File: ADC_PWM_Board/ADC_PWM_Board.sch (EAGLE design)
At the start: 52 parts, among them J1 22-05-7028-02, J10 22-05-7028-02, J11 22-05-7038-03, J2 22-05-7028-02, J3 22-05-7048-04, J4 22-05-7048-04, J5 22-05-7048-04, J6 22-05-7038-03, J7 22-05-7048-04, J8 22-05-7058-05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

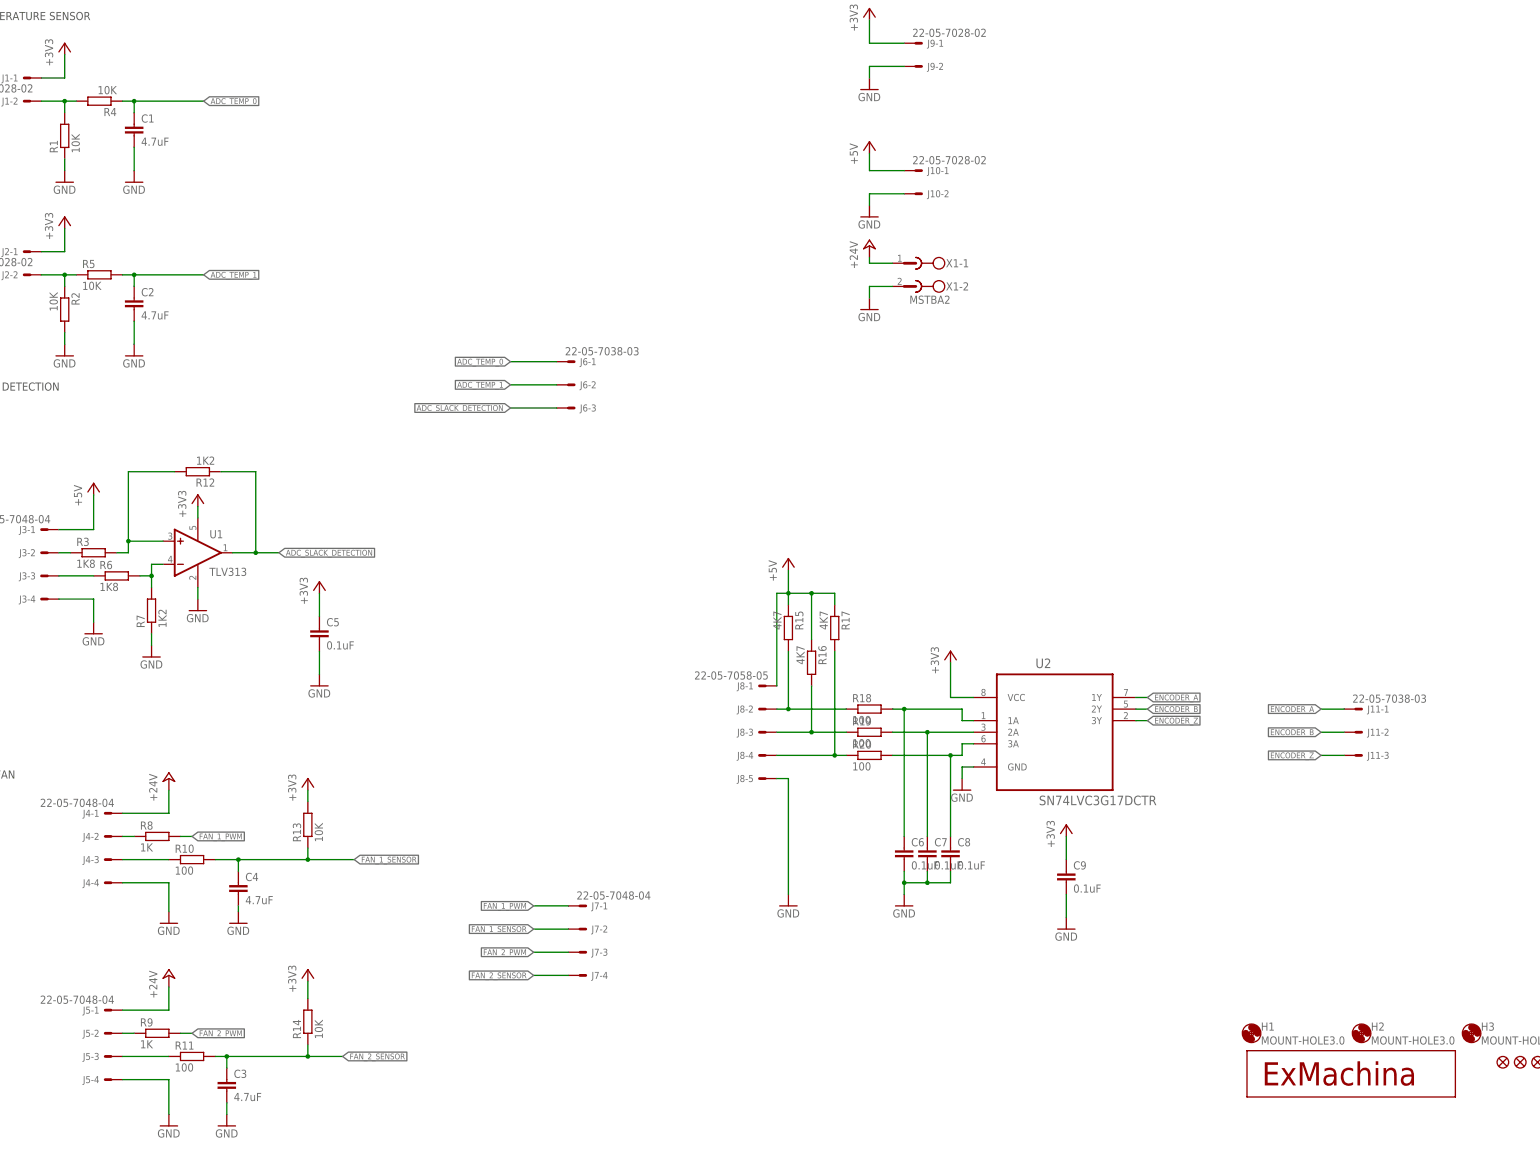
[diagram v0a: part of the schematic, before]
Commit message: Add opto to the Fan sensor and finsh to route it
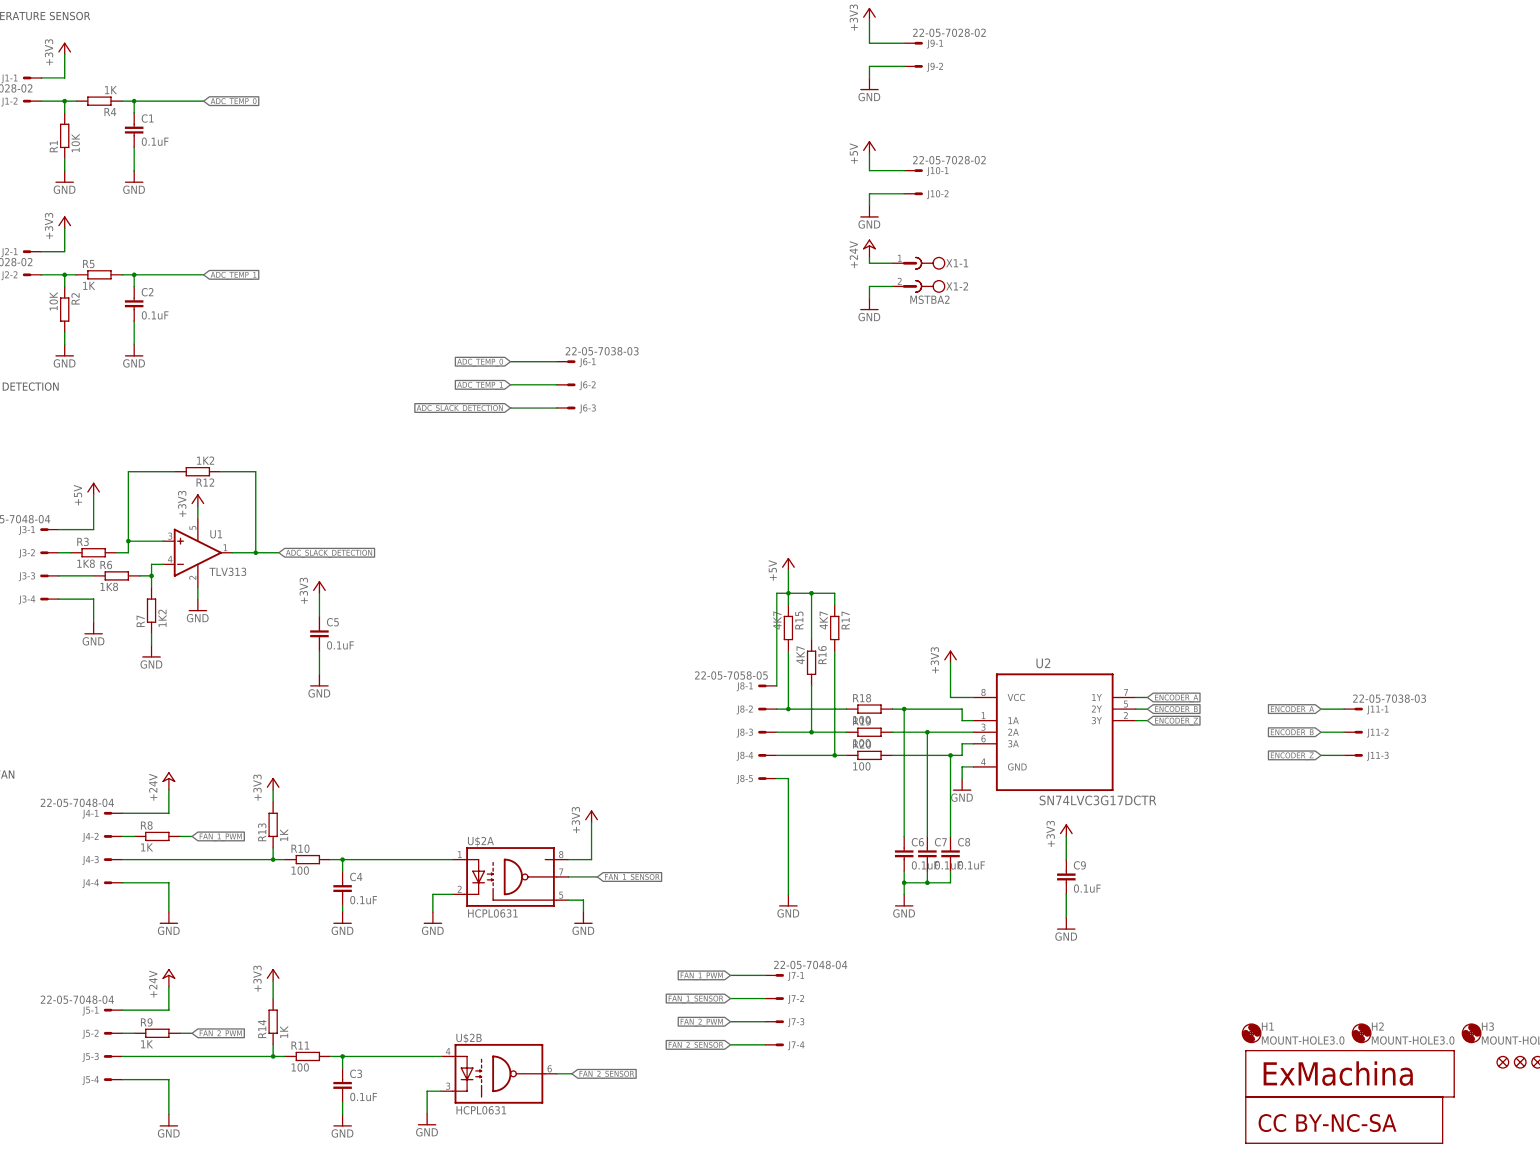
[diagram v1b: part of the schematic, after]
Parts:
- added U$1: CC-BY-NC-SA, cc-by-sa:CC-BY-NC-SA
- added U$2: HCPL0631, optocoupler:HCPL0631
- C1, C2, C3, C4: value 4.7uF -> 0.1uF
- R13, R14, R4, R5: value 10K -> 1K
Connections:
- removed net N$12: J5-3.S, R11.1
- removed net N$14: J4-3.S, R10.1
- new net N$1: J4-3.S, R10.1, R13.1
- new net N$2: J5-3.S, R11.1, R14.1
- new net N$3: C4.1, R10.2, U$2A.A1
- new net N$4: C3.1, R11.2, U$2B.A2
- net +3V3: now also U$2A.VCC
- net FAN_1_SENSOR: now also U$2A.VO; no longer C4.1, R10.2, R13.1
- net FAN_2_SENSOR: now also U$2B.VO2; no longer C3.1, R11.2, R14.1
- net GND: now also U$2A.C1, U$2A.GND, U$2B.C2
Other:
- moved on the sheet: C3, C4, J7-1, J7-2, J7-3, J7-4, R10, R11, R13, R14

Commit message: Add decoupling capacitor to the opto
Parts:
- C1, C2, C3, C4, C5, C6, C7, C8, C9: MPN (none) -> MC0603B104K250CT; OC_NEWARK (none) -> 06R4925
- H1, H2, H3, H4, JP1, JP2, JP3, JP4, T1, U$1: OC_NEWARK (none) -> unknown
- R1, R2: MPN (none) -> MCMR06X1002FTL; OC_NEWARK (none) -> 86T3506
- R10, R11, R18, R19, R20: MPN (none) -> MCMR06X1000FTL; OC_NEWARK (none) -> 86T3504
- R12, R7: MPN (none) -> MCMR06X1201FTL; OC_NEWARK (none) -> 86T3525
- R13, R14, R4, R5, R8, R9: MPN (none) -> MCMR06X1001FTL; OC_NEWARK (none) -> 86T3505
- R15, R16, R17: MPN (none) -> MCMR06X4701FTL; OC_NEWARK (none) -> 86T3649
- R3, R6: MPN (none) -> MCMR06X1801FTL; OC_NEWARK (none) -> 86T3556
- U$2: MPN (none) -> HCPL-0631-500E; OC_NEWARK (none) -> 52M7944
- U1: MPN (none) -> TLV313IDBVT; OC_NEWARK (none) -> 95Y0395
- U2: MF (none) -> TEXAS INSTRUMENTS

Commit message: Replacing name and value on the board
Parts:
- removed U$2: HCPL0631, optocoupler:HCPL0631
- removed X1: MSTBA2, con-phoenix-508:MSTBA2
- added C10: 0.1uF, rcl:C-EUC0603
- added J12: 22-05-7038-03, con-molex:22-05-7038-03
- added U3: SN74LVC3G17DCTR, ti:SN74LVC3G17DCTR
- J1, J10, J2, J9: MPN (none) -> 22-05-7028; OC_NEWARK (none) -> 25M1728
- J11: value 22-05-7038-03 -> MSTBA2; device con-molex:22-05-7038-03 -> con-phoenix-508:MSTBA2
- J3, J4, J5: MPN (none) -> 22-05-7048; OC_NEWARK (none) -> 26M6363
- J6: MPN (none) -> 22-05-7038; OC_NEWARK (none) -> 26M6362
- J7: value 22-05-7048-04 -> 22-05-7058-05; device con-molex:22-05-7048-04 -> con-molex:22-05-7058-05; MF (none) -> MOLEX; MPN (none) -> 22-05-7058; OC_NEWARK (none) -> 55H9619
- J8: value 22-05-7058-05 -> 22-05-7048-04; device con-molex:22-05-7058-05 -> con-molex:22-05-7048-04; MPN (none) -> 22-05-7048; OC_NEWARK (none) -> 26M6363
- R10: value 100 -> 1K2; MPN MCMR06X1000FTL -> MCMR06X1201FTL; OC_NEWARK 86T3504 -> 86T3525
- R11: value 100 -> 1K; MPN MCMR06X1000FTL -> MCMR06X1001FTL; OC_NEWARK 86T3504 -> 86T3505
- R12: value 1K2 -> 1K; MPN MCMR06X1201FTL -> MCMR06X1001FTL; OC_NEWARK 86T3525 -> 86T3505
- R13, R14: value 1K -> 100; MPN MCMR06X1001FTL -> MCMR06X1000FTL; OC_NEWARK 86T3505 -> 86T3504
- U2: value SN74LVC3G17DCTR -> HCPL0631; device ti:SN74LVC3G17DCTR -> optocoupler:HCPL0631; MF TEXAS INSTRUMENTS -> (none); MPN (none) -> HCPL-0631-500E; OC_NEWARK (none) -> 52M7944
- renumbered U$1 to CC1
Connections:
- net +24V: now also J11-1.1; no longer X1-1.1
- net +3V3: now also C10.1, C3.1, C6.1, R11.2, R12.2, U2A.VCC, U3.VCC; no longer C5.1, C9.1, R13.2, R14.2, U$2A.VCC, U2.VCC
- net +5V: now also J7-1.S; no longer J8-1.S
- net ADC_SLACK_DETECTION: now also R10.1; no longer R12.1
- net ENCODER_A: now also J12-1.S, U3.1Y; no longer J11-1.S, U2.1Y
- net ENCODER_B: now also J12-2.S, U3.2Y; no longer J11-2.S, U2.2Y
- net ENCODER_Z: now also J12-3.S, U3.3Y; no longer J11-3.S, U2.3Y
- net FAN_1_PWM: now also J8-1.S; no longer J7-1.S
- net FAN_1_SENSOR: now also J8-2.S, U2A.VO; no longer J7-2.S, U$2A.VO
- net FAN_2_PWM: now also J8-3.S; no longer J7-3.S
- net FAN_2_SENSOR: now also J8-4.S, U2B.VO2; no longer J7-4.S, U$2B.VO2
- net GND: now also C10.2, J11-2.1, J7-5.S, U2A.C1, U2A.GND, U2B.C2, U3.GND; no longer J8-5.S, U$2A.C1, U$2A.GND, U$2B.C2, U2.GND, X1-2.1
- net N$1: now also R11.1; no longer R10.1
- net N$2: now also R12.1; no longer R11.1
- net N$3: now also R13.2, U2A.A1; no longer R10.2, U$2A.A1
- net N$35: now also J7-2.S; no longer J8-2.S
- net N$4: now also C5.1, R14.2, U2B.A2; no longer C3.1, R11.2, U$2B.A2
- net N$40: now also J7-3.S; no longer J8-3.S
- net N$46: now also J7-4.S; no longer J8-4.S
- net N$52: now also C9.1, U3.3A; no longer C8.1, U2.3A
- net N$53: now also C8.1, U3.2A; no longer C7.1, U2.2A
- net N$54: now also C7.1, U3.1A; no longer C6.1, U2.1A
- net N$61: now also R10.2; no longer R12.2
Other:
- moved on the sheet: C3, C5, C6, C7, C8, C9, J7-1, J7-2, J7-3, J7-4, J8-1, J8-2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

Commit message: Rename fabrication folder
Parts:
- J10: value 22-05-7028-02 -> MSTBA2; device con-molex:22-05-7028-02 -> con-phoenix-508:MSTBA2; MPN 22-05-7028 -> (none); OC_NEWARK 25M1728 -> (none)
- J11: value MSTBA2 -> 22-05-7038-03; device con-phoenix-508:MSTBA2 -> con-molex:22-05-7038-03; MPN (none) -> 22-05-7038; OC_NEWARK (none) -> 26M6362
- R15, R16, R17: value 4K7 -> 2K7
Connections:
- new net AVDD: J1-1.S, J11-1.S, J2-1.S
- net +24V: now also J10-1.1; no longer J11-1.1
- net +3V3: now also J11-2.S; no longer J1-1.S, J2-1.S, J9-1.S
- net +5V: now also J7-4.S, J9-1.S; no longer J10-1.S, J7-1.S
- net GND: now also J10-2.1, J11-3.S, J7-1.S; no longer J10-2.S, J11-2.1, J7-5.S
- net N$35: now also J7-3.S; no longer J7-2.S
- net N$40: now also J7-5.S; no longer J7-3.S
- net N$46: now also J7-2.S; no longer J7-4.S
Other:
- moved on the sheet: J7-1, J7-2, J7-3, J7-4, J7-5, J9-1, J9-2
